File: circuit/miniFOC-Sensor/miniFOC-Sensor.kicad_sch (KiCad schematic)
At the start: 0 parts

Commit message: Complete the miniFOC-Sensor schematic drawing.
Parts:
- added C1: 10uF, Capacitor_SMD:C_0603_1608Metric, symbol Device:C
- added C2: 100nF, Capacitor_SMD:C_0603_1608Metric, symbol Device:C
- added J1: Conn_01x05, Connector_JST:JST_GH_SM05B-GHS-TB_1x05-1MP_P1.25mm_Horizontal, symbol Connector_Generic:Conn_01x05
- added U1: MT6701, Package_SO:SOP-8_3.9x4.9mm_P1.27mm, symbol Library:MT6701
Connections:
- new net +5V: C1.1, C2.1, J1.1 (Pin_1), U1.1 (VDD), U1.2 (MODE)
- new net GND: C1.2, C2.2, J1.5 (Pin_5), U1.4 (GND)
- new net SPI_CLK: J1.3 (Pin_3), U1.7 (CLK)
- new net SPI_CS: J1.4 (Pin_4), U1.8 (CSN)
- new net SPI_MISO: J1.2 (Pin_2), U1.6 (DO)
- no-connect marks 0 -> 2

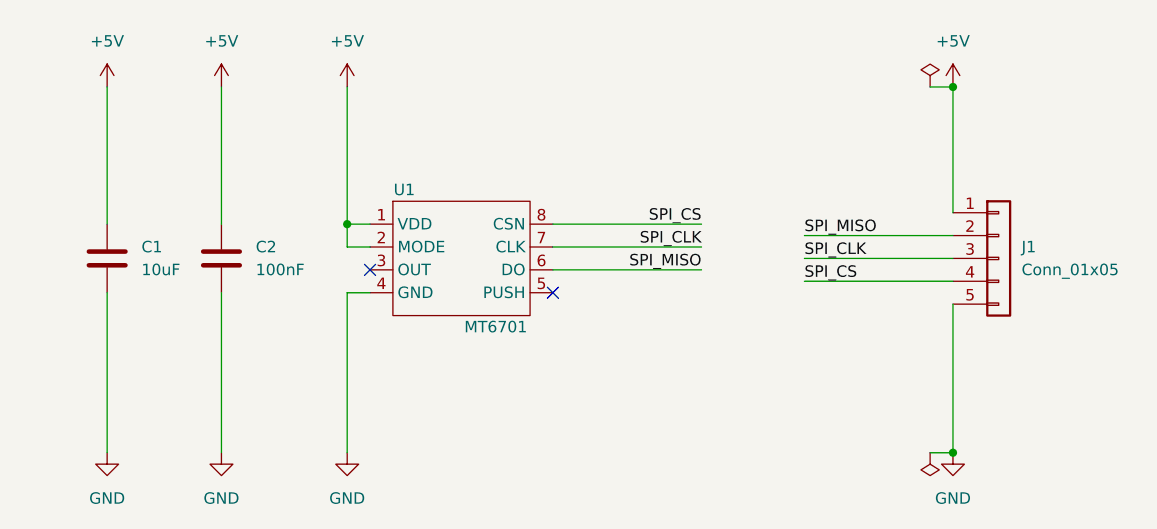
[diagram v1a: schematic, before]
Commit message: Completed PCB drawing of miniFOC sensor board
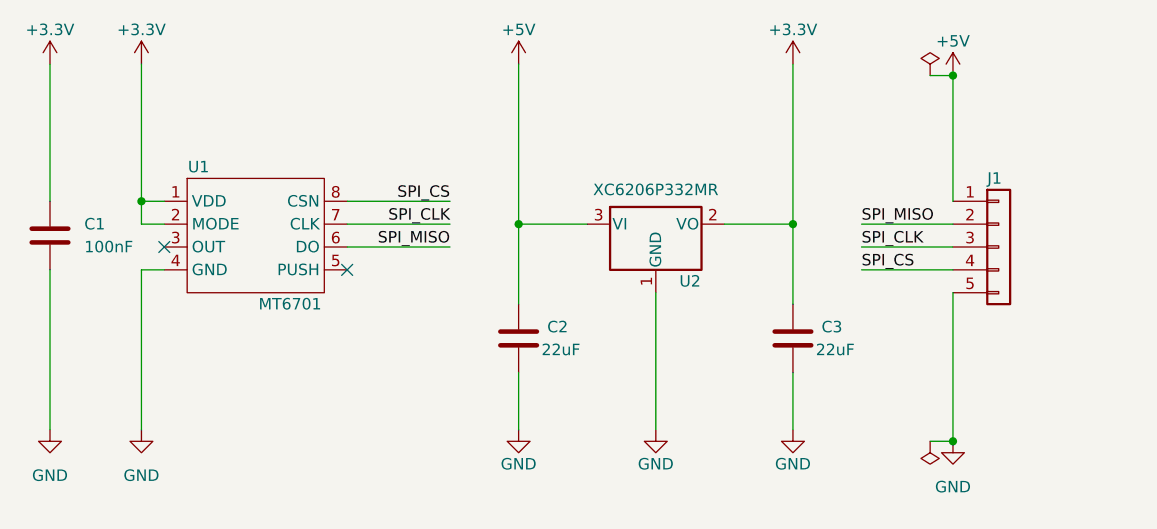
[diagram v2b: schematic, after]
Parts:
- removed C1: 10uF, Capacitor_SMD:C_0603_1608Metric, symbol Device:C
- added C2, C3: 22uF, Capacitor_SMD:C_0603_1608Metric, symbol Device:C
- added U2: XC6206P332MR, Package_TO_SOT_SMD:SOT-23, symbol Regulator_Linear:XC6206PxxxMR
- C1: renamed from C2; footprint Capacitor_SMD:C_0603_1608Metric -> Capacitor_SMD:C_0402_1005Metric
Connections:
- net +5V: now also C2.2, U2.3 (VI); no longer C1.1, U1.1 (VDD), U1.2 (MODE)
- net GND: now also C2.1, C3.1, U2.1 (GND)
- new net +3.3V: C1.1, C3.2, U1.1 (VDD), U1.2 (MODE), U2.2 (VO)
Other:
- moved on the sheet: C1, J1, U1

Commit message: Complete the circuit and PCB design for version 2.0.
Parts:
- C1: footprint Capacitor_SMD:C_0402_1005Metric -> Library:C_0402_1005Metric
- C2, C3: footprint Capacitor_SMD:C_0603_1608Metric -> Library:C_0603_1608Metric
- J1: footprint Connector_JST:JST_GH_SM05B-GHS-TB_1x05-1MP_P1.25mm_Horizontal -> Library:JST_GH_SM05B-GHS-TB_1x05-1MP_P1.25mm_Horizontal
- U1: footprint Package_SO:SOP-8_3.9x4.9mm_P1.27mm -> Library:SOP-8_3.9x4.9mm_P1.27mm
- U2: footprint Package_TO_SOT_SMD:SOT-23 -> Library:SOT-23
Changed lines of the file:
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@@
       (effects (font (size 1.27 1.27)) (justify left) hide)
     )
-    (property "Footprint" "Connector_JST:JST_GH_SM05B-GHS-TB_1x05-1MP_P1.25mm_Horizontal" (id 2) (at 203.2 104.14 0)
+    (property "Footprint" "Library:JST_GH_SM05B-GHS-TB_1x05-1MP_P1.25mm_Horizontal" (id 2) (at 203.2 104.14 0)
       (effects (font (size 1.27 1.27)) hide)
     )
@@
     (property "Reference" "U2" (id 0) (at 168.91 107.95 0))
     (property "Value" " XC6206P332MR" (id 1) (at 165.1 97.79 0))
-    (property "Footprint" "Package_TO_SOT_SMD:SOT-23" (id 2) (at 165.1 95.885 0)
+    (property "Footprint" "Library:SOT-23" (id 2) (at 165.1 95.885 0)
       (effects (font (size 1.27 1.27) italic) hide)
     )
@@
       (effects (font (size 1.27 1.27)) (justify right))
     )
-    (property "Footprint" "Capacitor_SMD:C_0603_1608Metric" (id 2) (at 179.3748 110.49 0)
+    (property "Footprint" "Library:C_0603_1608Metric" (id 2) (at 179.3748 110.49 0)
       (effects (font (size 1.27 1.27)) hide)
     )
@@
       (effects (font (size 1.27 1.27)) (justify right))
     )
-    (property "Footprint" "Capacitor_SMD:C_0603_1608Metric" (id 2) (at 148.8948 110.49 0)
+    (property "Footprint" "Library:C_0603_1608Metric" (id 2) (at 148.8948 110.49 0)
       (effects (font (size 1.27 1.27)) hide)
     )
@@
       (effects (font (size 1.27 1.27)) (justify left))
     )
-    (property "Footprint" "Capacitor_SMD:C_0402_1005Metric" (id 2) (at 98.7552 106.68 0)
+    (property "Footprint" "Library:C_0402_1005Metric" (id 2) (at 98.7552 106.68 0)
       (effects (font (size 1.27 1.27)) hide)
     )
@@
     (property "Reference" "U1" (id 0) (at 114.3 95.25 0))
     (property "Value" "MT6701" (id 1) (at 124.46 110.49 0))
-    (property "Footprint" "Package_SO:SOP-8_3.9x4.9mm_P1.27mm" (id 2) (at 119.38 113.03 0)
+    (property "Footprint" "Library:SOP-8_3.9x4.9mm_P1.27mm" (id 2) (at 119.38 113.03 0)
       (effects (font (size 1.27 1.27)) hide)
     )
@@
     )
     (path "/7d076eb0-75c0-4f9c-8d7e-fedd011efafb"
-      (reference "C1") (unit 1) (value "100nF") (footprint "Capacitor_SMD:C_0402_1005Metric")
+      (reference "C1") (unit 1) (value "100nF") (footprint "Library:C_0402_1005Metric")
     )
     (path "/780f217e-c351-47a5-b96e-435b7e82040a"
-      (reference "C2") (unit 1) (value "22uF") (footprint "Capacitor_SMD:C_0603_1608Metric")
+      (reference "C2") (unit 1) (value "22uF") (footprint "Library:C_0603_1608Metric")
     )
     (path "/2cb7744d-7fa3-4158-9ecd-73a1870a8077"
-      (reference "C3") (unit 1) (value "22uF") (footprint "Capacitor_SMD:C_0603_1608Metric")
+      (reference "C3") (unit 1) (value "22uF") (footprint "Library:C_0603_1608Metric")
     )
     (path "/042e549c-9325-4b88-91e1-c7ebd08b5658"
-      (reference "J1") (unit 1) (value "Conn_01x05") (footprint "Connector_JST:JST_GH_SM05B-GHS-TB_1x05-1MP_P1.25mm_Horizontal")
+      (reference "J1") (unit 1) (value "Conn_01x05") (footprint "Library:JST_GH_SM05B-GHS-TB_1x05-1MP_P1.25mm_Horizontal")
     )
     (path "/c140bfcf-f85b-4b10-b5ad-46ad5065a32d"
-      (reference "U1") (unit 1) (value "MT6701") (footprint "Package_SO:SOP-8_3.9x4.9mm_P1.27mm")
+      (reference "U1") (unit 1) (value "MT6701") (footprint "Library:SOP-8_3.9x4.9mm_P1.27mm")
     )
     (path "/1495fbbd-7478-4f4a-81bb-8f27be4946d9"
-      (reference "U2") (unit 1) (value " XC6206P332MR") (footprint "Package_TO_SOT_SMD:SOT-23")
-    )
-  )
+      (reference "U2") (unit 1) (value " XC6206P332MR") (footprint "Library:SOT-23")
+    )
+  )
